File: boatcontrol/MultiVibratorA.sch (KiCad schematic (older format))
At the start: 5 parts, among them IC401 CD74HCT221E, U2103 74HC86

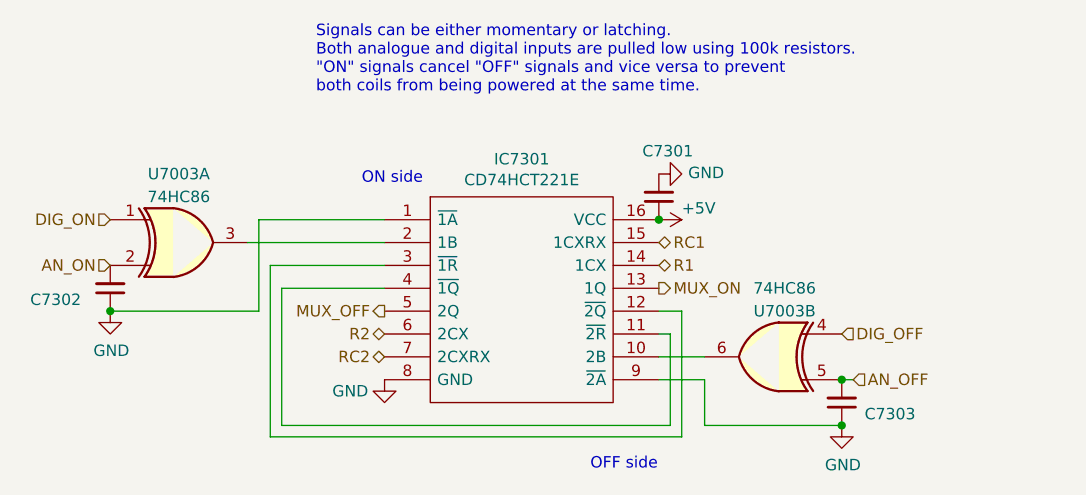
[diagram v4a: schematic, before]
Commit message: Switch to common 5v 10K ohm for an sigs
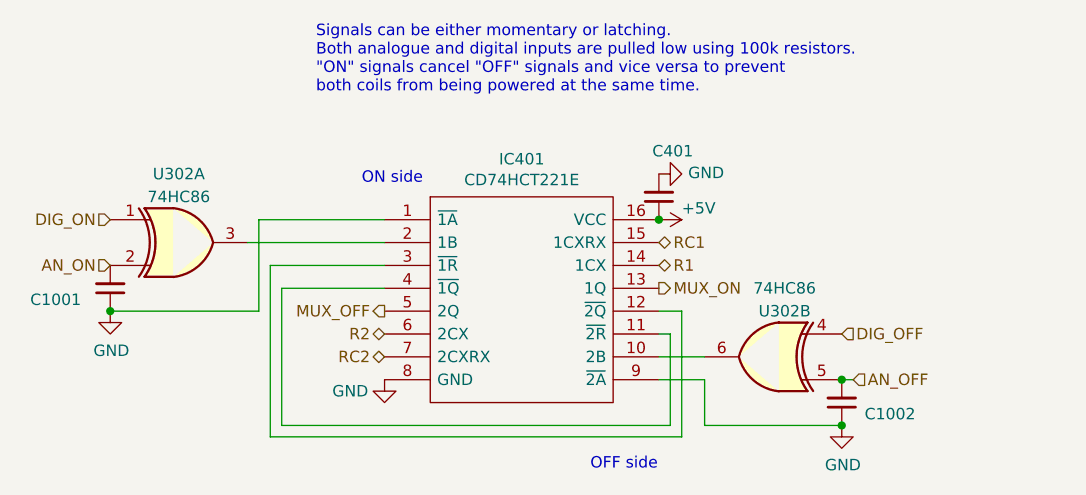
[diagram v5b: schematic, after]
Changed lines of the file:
@@
 $Descr A4 11693 8268
 encoding utf-8
-Sheet 65 97
+Sheet 10 97
 Title "Boat Control Hat"
 Date ""
@@
 AR Path="/D1BB8DB4/5F75E923/604747F3/603A29DF" Ref="IC7301"  Part="1"
 AR Path="/D1BB8DB4/5F75E923/604747FF/603A29DF" Ref="IC7401"  Part="1"
-F 0 "IC7301" H 5450 4215 50  0000 C CNN
+F 0 "IC401" H 5450 4215 50  0000 C CNN
 F 1 "CD74HCT221E" H 5450 4124 50  0000 C CNN
 F 2 "DIP794W53P254L1930H508Q16N" H 5900 4050 50  0001 L CNN
@@
 AR Path="/D1BB8DB4/5F75E923/604747F3/5FDA22CD" Ref="#PWR07302"  Part="1"
 AR Path="/D1BB8DB4/5F75E923/604747FF/5FDA22CD" Ref="#PWR07402"  Part="1"
-F 0 "#PWR07302" H 4850 4400 50  0001 C CNN
+F 0 "#PWR0402" H 4850 4400 50  0001 C CNN
 F 1 "GND" H 4700 4600 50  0000 C CNN
 F 2 "" H 4850 4650 50  0001 C CNN
@@
 AR Path="/D1BB8DB4/5F75E923/604747F3/603A29E0" Ref="#PWR07301"  Part="1"
 AR Path="/D1BB8DB4/5F75E923/604747FF/603A29E0" Ref="#PWR07401"  Part="1"
-F 0 "#PWR07301" H 6050 3800 50  0001 C CNN
+F 0 "#PWR0401" H 6050 3800 50  0001 C CNN
 F 1 "+5V" V 6000 4050 50  0000 L CNN
 F 2 "" H 6050 3950 50  0001 C CNN
@@
 AR Path="/D1BB8DB4/5F317CB5/60365B0F/603A29E9" Ref="#PWR0183"  Part="1"
 AR Path="/D1BB8DB4/5F317CB5/60365B35/603A29E9" Ref="#PWR0185"  Part="1"
-F 0 "#PWR0181" H 6050 3500 50  0001 C CNN
+F 0 "#PWR0155" H 6050 3500 50  0001 C CNN
 F 1 "GND" V 6055 3622 50  0000 R CNN
 F 2 "" H 6050 3750 50  0001 C CNN
@@
 AR Path="/D1BB8DB4/5F317CB5/60365B0F/603A29E8" Ref="C8001"  Part="1"
 AR Path="/D1BB8DB4/5F317CB5/60365B35/603A29E8" Ref="C8201"  Part="1"
-F 0 "C7301" H 5900 3650 50  0000 L CNN
+F 0 "C401" H 5900 3650 50  0000 L CNN
 F 1 "0.1μF" H 6141 3805 50  0001 L CNN
 F 2 "Capacitor_THT:C_Disc_D7.5mm_W5.0mm_P5.00mm" H 6050 3850 50  0001 C CNN
@@
 AR Path="/D1BB8DB4/5F75E923/604747F3/60314A10" Ref="C7303"  Part="1"
 AR Path="/D1BB8DB4/5F317CB5/60365B35/60314A10" Ref="C8203"  Part="1"
-F 0 "C7303" H 6950 4800 50  0000 L CNN
+F 0 "C1002" H 6950 4800 50  0000 L CNN
 F 1 "1µF" H 6000 4650 50  0001 L CNN
 F 2 "Capacitor_THT:C_Disc_D7.5mm_W5.0mm_P5.00mm" H 6850 4750 50  0001 C CNN
@@
 AR Path="/D1BB8DB4/5F75E923/604747F3/602124D8" Ref="#PWR0337"  Part="1"
 AR Path="/D1BB8DB4/5F317CB5/60365B35/602124D8" Ref="#PWR0352"  Part="1"
-F 0 "#PWR0337" H 6850 4600 50  0001 C CNN
+F 0 "#PWR0255" H 6850 4600 50  0001 C CNN
 F 1 "GND" H 6855 4677 50  0000 C CNN
 F 2 "" H 6850 4850 50  0001 C CNN
@@
 AR Path="/D1BB8DB4/5F75E923/604747F3/60416EE6" Ref="U7003"  Part="1"
 AR Path="/D1BB8DB4/5F317CB5/60365B35/60416EE6" Ref="U7903"  Part="1"
-F 0 "U7003" H 3950 4350 50  0000 C CNN
+F 0 "U302" H 3950 4350 50  0000 C CNN
 F 1 "74HC86" H 3950 4250 50  0000 C CNN
 F 2 "" H 3950 4050 50  0001 C CNN
@@
 AR Path="/D1BB8DB4/5F75E923/604747F3/603A29E5" Ref="#PWR0338"  Part="1"
 AR Path="/D1BB8DB4/5F317CB5/60365B35/603A29E5" Ref="#PWR0353"  Part="1"
-F 0 "#PWR0338" H 3650 4100 50  0001 C CNN
+F 0 "#PWR0256" H 3650 4100 50  0001 C CNN
 F 1 "GND" H 3655 4177 50  0000 C CNN
 F 2 "" H 3650 4350 50  0001 C CNN
@@
 AR Path="/D1BB8DB4/5F75E923/604747F3/60314A12" Ref="C7302"  Part="1"
 AR Path="/D1BB8DB4/5F317CB5/60365B35/60314A12" Ref="C8202"  Part="1"
-F 0 "C7302" H 3300 4300 50  0000 L CNN
+F 0 "C1001" H 3300 4300 50  0000 L CNN
 F 1 "1µF" H 2800 4150 50  0001 L CNN
 F 2 "Capacitor_THT:C_Disc_D7.5mm_W5.0mm_P5.00mm" H 3650 4250 50  0001 C CNN
@@
 AR Path="/D1BB8DB4/5F75E923/604747F3/60491845" Ref="U7003"  Part="2"
 AR Path="/D1BB8DB4/5F317CB5/60365B35/60491845" Ref="U7903"  Part="2"
-F 0 "U7003" H 6500 4750 50  0000 C CNN
+F 0 "U302" H 6500 4750 50  0000 C CNN
 F 1 "74HC86" H 6500 4850 50  0000 C CNN
 F 2 "" H 6550 4550 50  0001 C CNN

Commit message: Add caps for xors
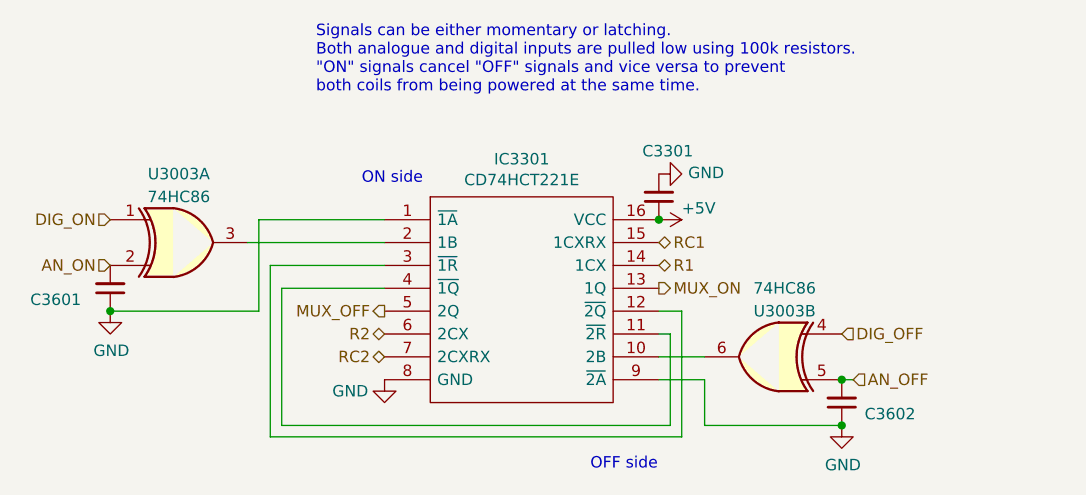
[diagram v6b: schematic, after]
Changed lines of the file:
@@
 $Descr A4 11693 8268
 encoding utf-8
-Sheet 10 97
+Sheet 36 97
 Title "Boat Control Hat"
 Date ""
@@
 AR Path="/D1BB8DB4/5F75E923/604747F3/603A29DF" Ref="IC7301"  Part="1"
 AR Path="/D1BB8DB4/5F75E923/604747FF/603A29DF" Ref="IC7401"  Part="1"
-F 0 "IC401" H 5450 4215 50  0000 C CNN
+F 0 "IC3301" H 5450 4215 50  0000 C CNN
 F 1 "CD74HCT221E" H 5450 4124 50  0000 C CNN
 F 2 "DIP794W53P254L1930H508Q16N" H 5900 4050 50  0001 L CNN
@@
 AR Path="/D1BB8DB4/5F75E923/604747F3/5FDA22CD" Ref="#PWR07302"  Part="1"
 AR Path="/D1BB8DB4/5F75E923/604747FF/5FDA22CD" Ref="#PWR07402"  Part="1"
-F 0 "#PWR0402" H 4850 4400 50  0001 C CNN
+F 0 "#PWR03302" H 4850 4400 50  0001 C CNN
 F 1 "GND" H 4700 4600 50  0000 C CNN
 F 2 "" H 4850 4650 50  0001 C CNN
@@
 AR Path="/D1BB8DB4/5F75E923/604747F3/603A29E0" Ref="#PWR07301"  Part="1"
 AR Path="/D1BB8DB4/5F75E923/604747FF/603A29E0" Ref="#PWR07401"  Part="1"
-F 0 "#PWR0401" H 6050 3800 50  0001 C CNN
+F 0 "#PWR03301" H 6050 3800 50  0001 C CNN
 F 1 "+5V" V 6000 4050 50  0000 L CNN
 F 2 "" H 6050 3950 50  0001 C CNN
@@
 AR Path="/D1BB8DB4/5F317CB5/60365B0F/603A29E9" Ref="#PWR0183"  Part="1"
 AR Path="/D1BB8DB4/5F317CB5/60365B35/603A29E9" Ref="#PWR0185"  Part="1"
-F 0 "#PWR0155" H 6050 3500 50  0001 C CNN
+F 0 "#PWR0169" H 6050 3500 50  0001 C CNN
 F 1 "GND" V 6055 3622 50  0000 R CNN
 F 2 "" H 6050 3750 50  0001 C CNN
@@
 AR Path="/D1BB8DB4/5F317CB5/60365B0F/603A29E8" Ref="C8001"  Part="1"
 AR Path="/D1BB8DB4/5F317CB5/60365B35/603A29E8" Ref="C8201"  Part="1"
-F 0 "C401" H 5900 3650 50  0000 L CNN
+F 0 "C3301" H 5900 3650 50  0000 L CNN
 F 1 "0.1μF" H 6141 3805 50  0001 L CNN
 F 2 "Capacitor_THT:C_Disc_D7.5mm_W5.0mm_P5.00mm" H 6050 3850 50  0001 C CNN
@@
 AR Path="/D1BB8DB4/5F75E923/604747F3/60314A10" Ref="C7303"  Part="1"
 AR Path="/D1BB8DB4/5F317CB5/60365B35/60314A10" Ref="C8203"  Part="1"
-F 0 "C1002" H 6950 4800 50  0000 L CNN
+F 0 "C3602" H 6950 4800 50  0000 L CNN
 F 1 "1µF" H 6000 4650 50  0001 L CNN
 F 2 "Capacitor_THT:C_Disc_D7.5mm_W5.0mm_P5.00mm" H 6850 4750 50  0001 C CNN
@@
 AR Path="/D1BB8DB4/5F75E923/604747F3/602124D8" Ref="#PWR0337"  Part="1"
 AR Path="/D1BB8DB4/5F317CB5/60365B35/602124D8" Ref="#PWR0352"  Part="1"
-F 0 "#PWR0255" H 6850 4600 50  0001 C CNN
+F 0 "#PWR0295" H 6850 4600 50  0001 C CNN
 F 1 "GND" H 6855 4677 50  0000 C CNN
 F 2 "" H 6850 4850 50  0001 C CNN
@@
 AR Path="/D1BB8DB4/5F75E923/604747F3/60416EE6" Ref="U7003"  Part="1"
 AR Path="/D1BB8DB4/5F317CB5/60365B35/60416EE6" Ref="U7903"  Part="1"
-F 0 "U302" H 3950 4350 50  0000 C CNN
+F 0 "U3003" H 3950 4350 50  0000 C CNN
 F 1 "74HC86" H 3950 4250 50  0000 C CNN
 F 2 "" H 3950 4050 50  0001 C CNN
@@
 AR Path="/D1BB8DB4/5F75E923/604747F3/603A29E5" Ref="#PWR0338"  Part="1"
 AR Path="/D1BB8DB4/5F317CB5/60365B35/603A29E5" Ref="#PWR0353"  Part="1"
-F 0 "#PWR0256" H 3650 4100 50  0001 C CNN
+F 0 "#PWR0296" H 3650 4100 50  0001 C CNN
 F 1 "GND" H 3655 4177 50  0000 C CNN
 F 2 "" H 3650 4350 50  0001 C CNN
@@
 AR Path="/D1BB8DB4/5F75E923/604747F3/60314A12" Ref="C7302"  Part="1"
 AR Path="/D1BB8DB4/5F317CB5/60365B35/60314A12" Ref="C8202"  Part="1"
-F 0 "C1001" H 3300 4300 50  0000 L CNN
+F 0 "C3601" H 3300 4300 50  0000 L CNN
 F 1 "1µF" H 2800 4150 50  0001 L CNN
 F 2 "Capacitor_THT:C_Disc_D7.5mm_W5.0mm_P5.00mm" H 3650 4250 50  0001 C CNN
@@
 AR Path="/D1BB8DB4/5F75E923/604747F3/60491845" Ref="U7003"  Part="2"
 AR Path="/D1BB8DB4/5F317CB5/60365B35/60491845" Ref="U7903"  Part="2"
-F 0 "U302" H 6500 4750 50  0000 C CNN
+F 0 "U3003" H 6500 4750 50  0000 C CNN
 F 1 "74HC86" H 6500 4850 50  0000 C CNN
 F 2 "" H 6550 4550 50  0001 C CNN

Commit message: Sorted Caps
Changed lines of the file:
@@
 $Descr A4 11693 8268
 encoding utf-8
-Sheet 36 97
+Sheet 41 97
 Title "Boat Control Hat"
 Date ""
@@
 AR Path="/D1BB8DB4/5F75E923/604747F3/603A29DF" Ref="IC7301"  Part="1"
 AR Path="/D1BB8DB4/5F75E923/604747FF/603A29DF" Ref="IC7401"  Part="1"
-F 0 "IC3301" H 5450 4215 50  0000 C CNN
+F 0 "IC5301" H 5450 4215 50  0000 C CNN
 F 1 "CD74HCT221E" H 5450 4124 50  0000 C CNN
 F 2 "DIP794W53P254L1930H508Q16N" H 5900 4050 50  0001 L CNN
@@
 AR Path="/D1BB8DB4/5F75E923/604747F3/5FDA22CD" Ref="#PWR07302"  Part="1"
 AR Path="/D1BB8DB4/5F75E923/604747FF/5FDA22CD" Ref="#PWR07402"  Part="1"
-F 0 "#PWR03302" H 4850 4400 50  0001 C CNN
+F 0 "#PWR05302" H 4850 4400 50  0001 C CNN
 F 1 "GND" H 4700 4600 50  0000 C CNN
 F 2 "" H 4850 4650 50  0001 C CNN
@@
 AR Path="/D1BB8DB4/5F75E923/604747F3/603A29E0" Ref="#PWR07301"  Part="1"
 AR Path="/D1BB8DB4/5F75E923/604747FF/603A29E0" Ref="#PWR07401"  Part="1"
-F 0 "#PWR03301" H 6050 3800 50  0001 C CNN
+F 0 "#PWR05301" H 6050 3800 50  0001 C CNN
 F 1 "+5V" V 6000 4050 50  0000 L CNN
 F 2 "" H 6050 3950 50  0001 C CNN
@@
 AR Path="/D1BB8DB4/5F317CB5/60365B0F/603A29E9" Ref="#PWR0183"  Part="1"
 AR Path="/D1BB8DB4/5F317CB5/60365B35/603A29E9" Ref="#PWR0185"  Part="1"
-F 0 "#PWR0169" H 6050 3500 50  0001 C CNN
+F 0 "#PWR0171" H 6050 3500 50  0001 C CNN
 F 1 "GND" V 6055 3622 50  0000 R CNN
 F 2 "" H 6050 3750 50  0001 C CNN
@@
 AR Path="/D1BB8DB4/5F317CB5/60365B0F/603A29E8" Ref="C8001"  Part="1"
 AR Path="/D1BB8DB4/5F317CB5/60365B35/603A29E8" Ref="C8201"  Part="1"
-F 0 "C3301" H 5900 3650 50  0000 L CNN
+F 0 "C5301" H 5900 3650 50  0000 L CNN
 F 1 "0.1μF" H 6141 3805 50  0001 L CNN
 F 2 "Capacitor_THT:C_Disc_D7.5mm_W5.0mm_P5.00mm" H 6050 3850 50  0001 C CNN
@@
 AR Path="/D1BB8DB4/5F75E923/604747F3/60314A10" Ref="C7303"  Part="1"
 AR Path="/D1BB8DB4/5F317CB5/60365B35/60314A10" Ref="C8203"  Part="1"
-F 0 "C3602" H 6950 4800 50  0000 L CNN
+F 0 "C5303" H 6950 4800 50  0000 L CNN
 F 1 "1µF" H 6000 4650 50  0001 L CNN
 F 2 "Capacitor_THT:C_Disc_D7.5mm_W5.0mm_P5.00mm" H 6850 4750 50  0001 C CNN
@@
 AR Path="/D1BB8DB4/5F75E923/604747F3/602124D8" Ref="#PWR0337"  Part="1"
 AR Path="/D1BB8DB4/5F317CB5/60365B35/602124D8" Ref="#PWR0352"  Part="1"
-F 0 "#PWR0295" H 6850 4600 50  0001 C CNN
+F 0 "#PWR0311" H 6850 4600 50  0001 C CNN
 F 1 "GND" H 6855 4677 50  0000 C CNN
 F 2 "" H 6850 4850 50  0001 C CNN
@@
 AR Path="/D1BB8DB4/5F75E923/604747F3/60416EE6" Ref="U7003"  Part="1"
 AR Path="/D1BB8DB4/5F317CB5/60365B35/60416EE6" Ref="U7903"  Part="1"
-F 0 "U3003" H 3950 4350 50  0000 C CNN
+F 0 "U4002" H 3950 4350 50  0000 C CNN
 F 1 "74HC86" H 3950 4250 50  0000 C CNN
 F 2 "" H 3950 4050 50  0001 C CNN
@@
 AR Path="/D1BB8DB4/5F75E923/604747F3/603A29E5" Ref="#PWR0338"  Part="1"
 AR Path="/D1BB8DB4/5F317CB5/60365B35/603A29E5" Ref="#PWR0353"  Part="1"
-F 0 "#PWR0296" H 3650 4100 50  0001 C CNN
+F 0 "#PWR0312" H 3650 4100 50  0001 C CNN
 F 1 "GND" H 3655 4177 50  0000 C CNN
 F 2 "" H 3650 4350 50  0001 C CNN
@@
 AR Path="/D1BB8DB4/5F75E923/604747F3/60314A12" Ref="C7302"  Part="1"
 AR Path="/D1BB8DB4/5F317CB5/60365B35/60314A12" Ref="C8202"  Part="1"
-F 0 "C3601" H 3300 4300 50  0000 L CNN
+F 0 "C5302" H 3300 4300 50  0000 L CNN
 F 1 "1µF" H 2800 4150 50  0001 L CNN
 F 2 "Capacitor_THT:C_Disc_D7.5mm_W5.0mm_P5.00mm" H 3650 4250 50  0001 C CNN
@@
 AR Path="/D1BB8DB4/5F75E923/604747F3/60491845" Ref="U7003"  Part="2"
 AR Path="/D1BB8DB4/5F317CB5/60365B35/60491845" Ref="U7903"  Part="2"
-F 0 "U3003" H 6500 4750 50  0000 C CNN
+F 0 "U4002" H 6500 4750 50  0000 C CNN
 F 1 "74HC86" H 6500 4850 50  0000 C CNN
 F 2 "" H 6550 4550 50  0001 C CNN
